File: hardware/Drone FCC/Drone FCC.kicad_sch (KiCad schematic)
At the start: 4 parts

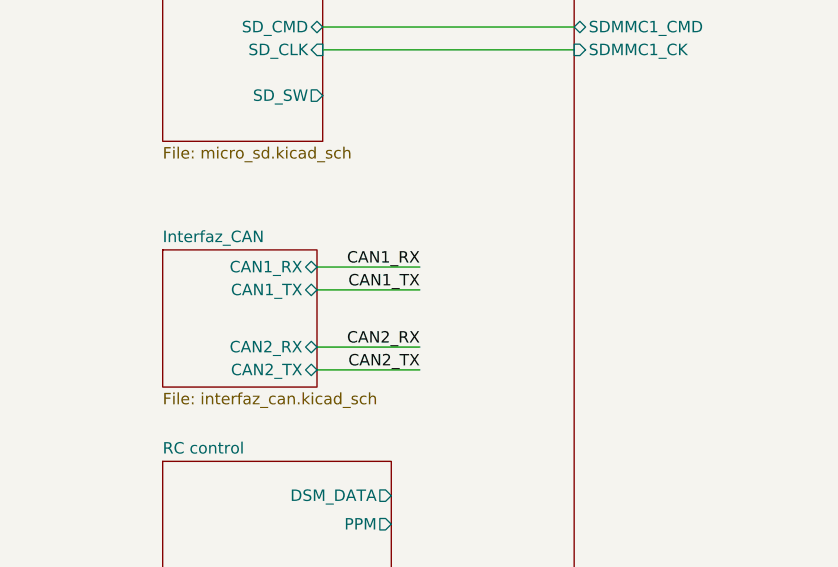
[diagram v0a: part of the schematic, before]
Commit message: add CAN schematic
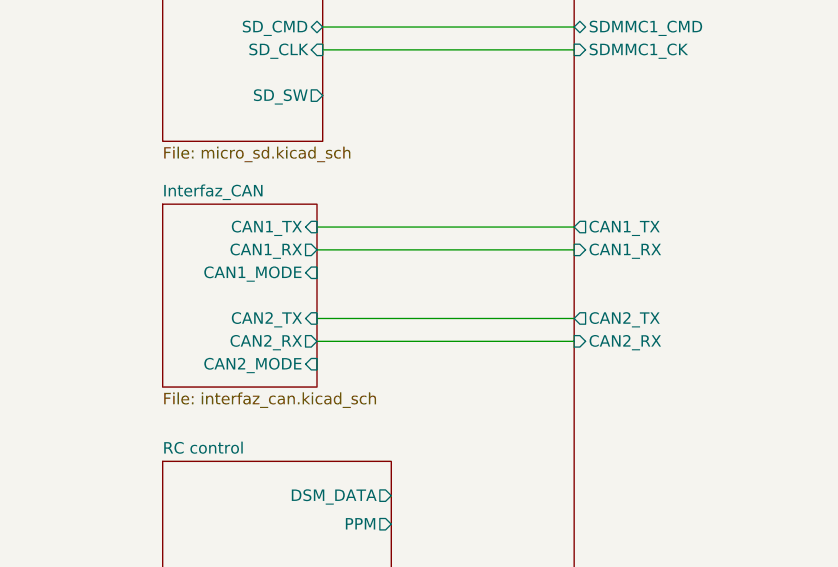
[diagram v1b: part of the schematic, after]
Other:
- sheet Interfaz_CAN ports: added CAN1_MODE, CAN2_MODE; removed none
- sheet MCU ports: added CAN1_RX, CAN1_TX, CAN2_RX, CAN2_TX; removed none

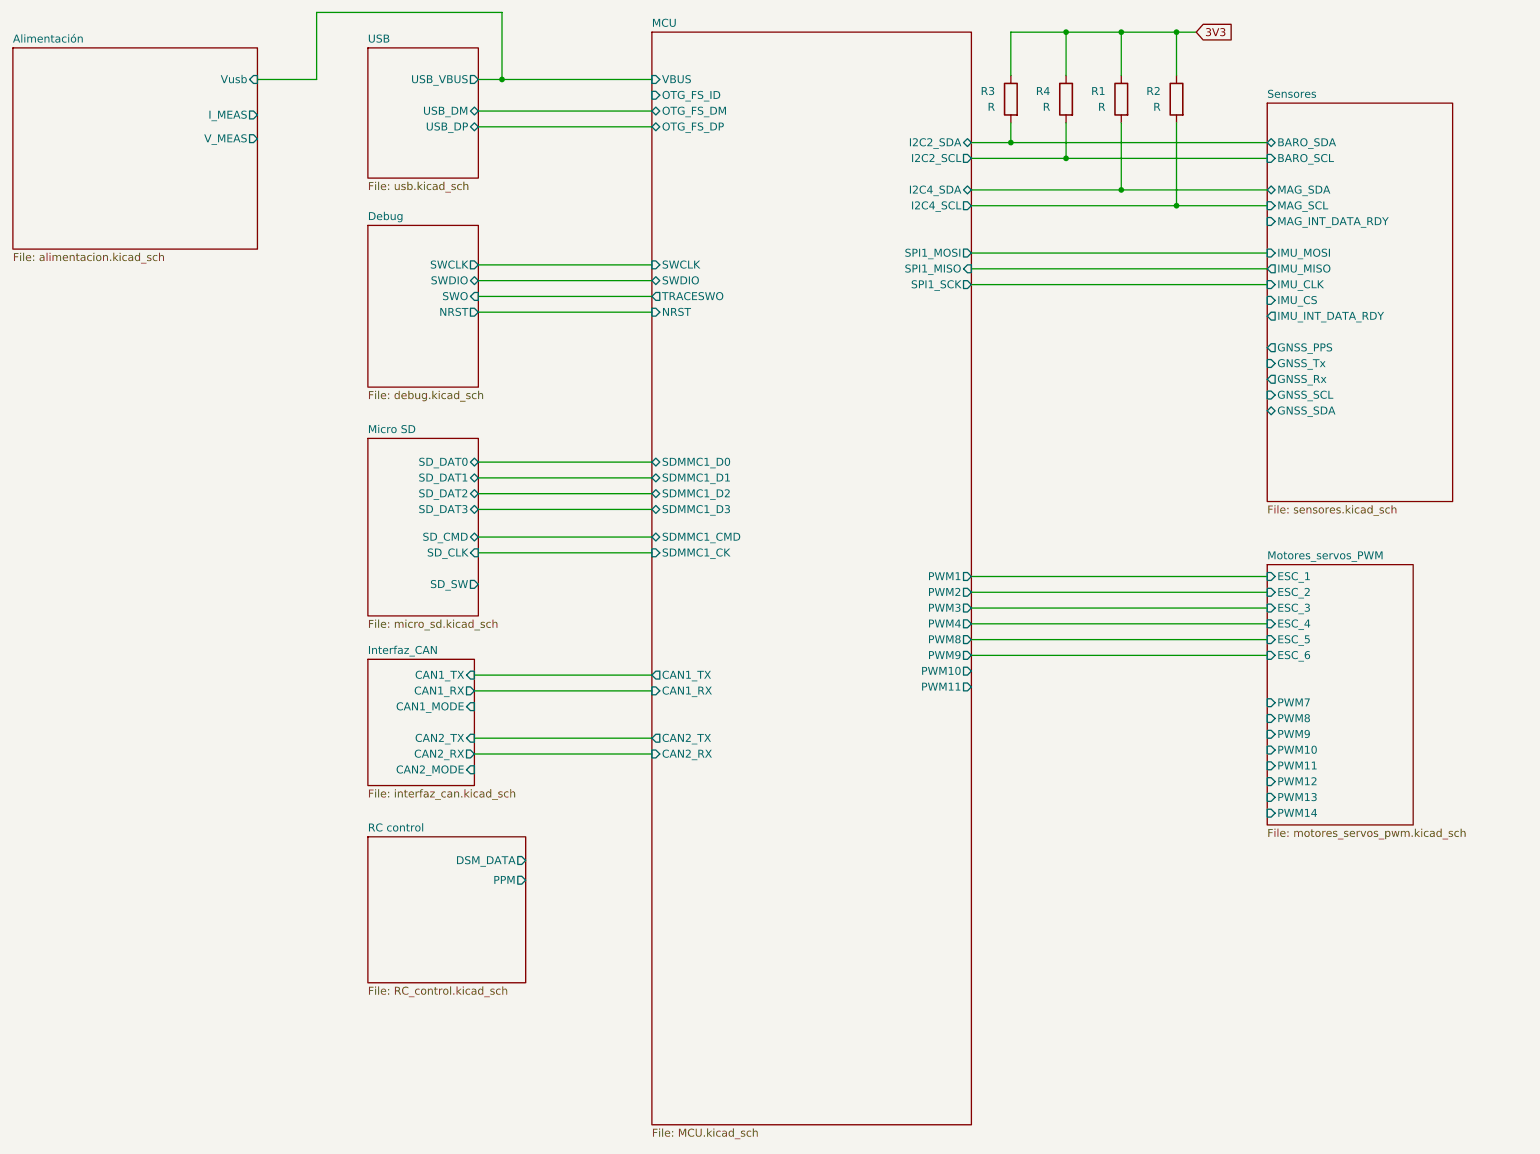
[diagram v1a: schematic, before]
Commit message: rearranged FCC schematic
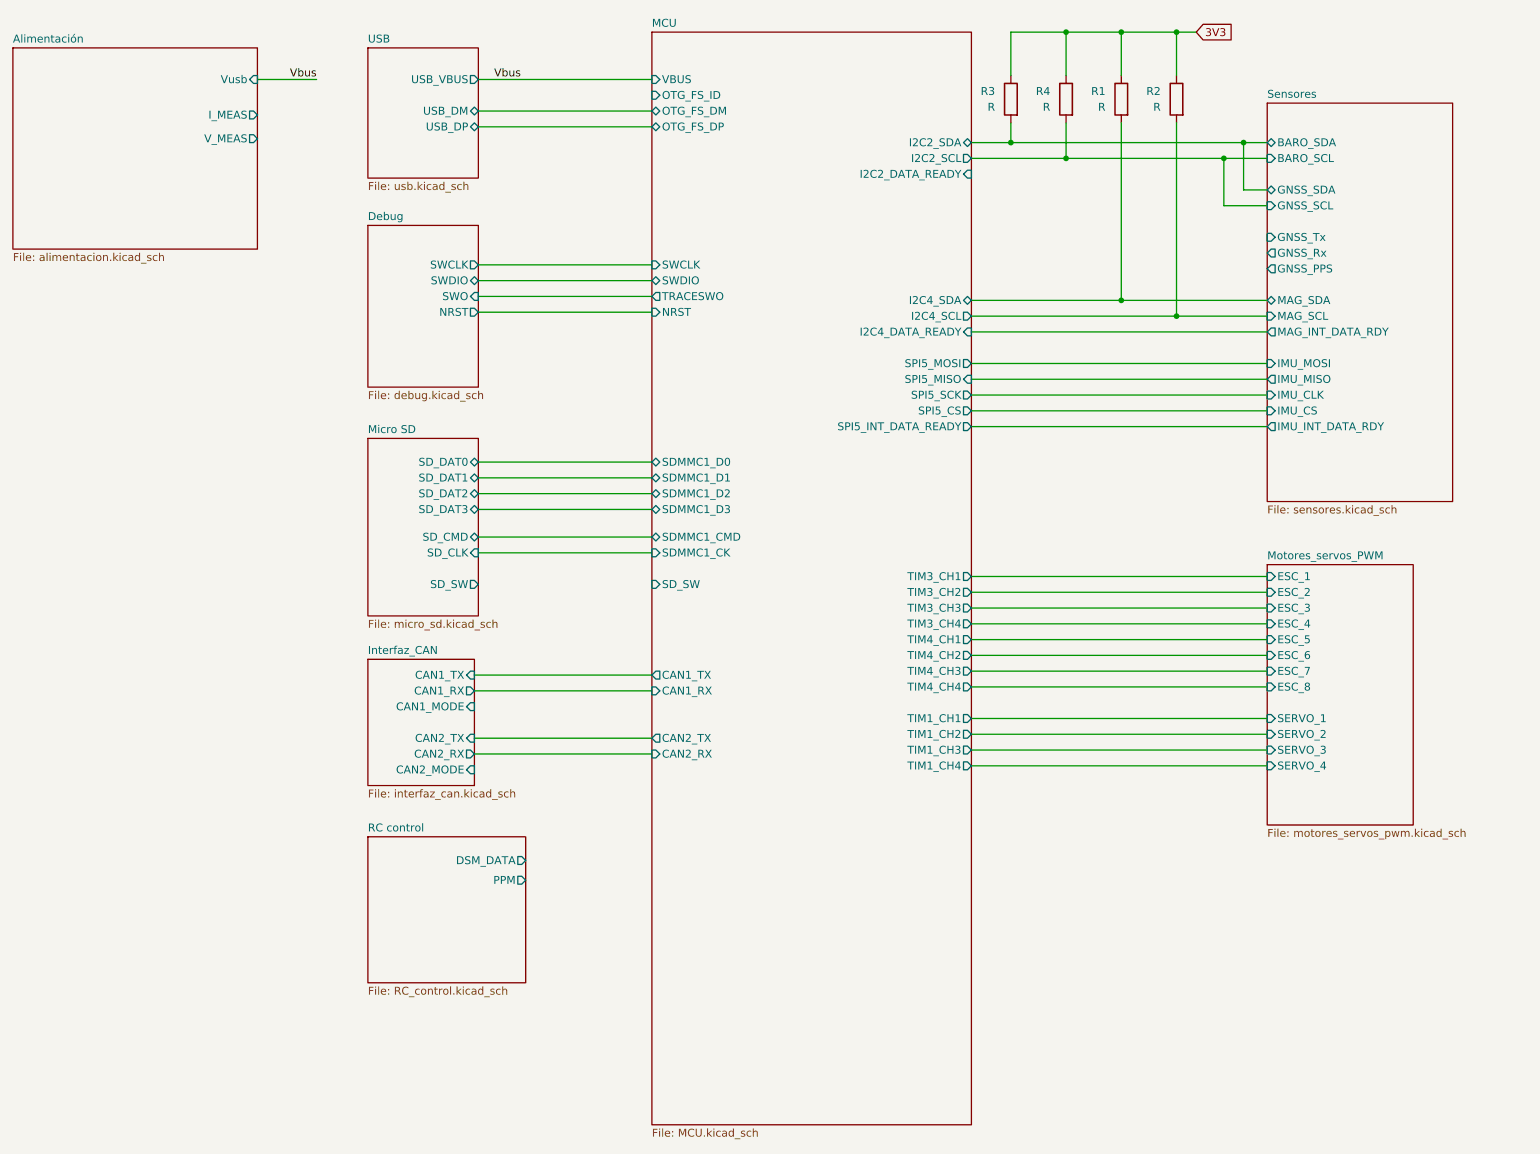
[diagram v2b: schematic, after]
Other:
- sheet MCU ports: added I2C2_DATA_READY, I2C4_DATA_READY, SD_SW, SPI5_CS, SPI5_INT_DATA_READY, SPI5_MISO, SPI5_MOSI, SPI5_SCK, TIM1_CH1, TIM1_CH2, TIM1_CH3, TIM1_CH4, TIM3_CH1, TIM3_CH2, TIM3_CH3, TIM3_CH4, TIM4_CH1, TIM4_CH2, TIM4_CH3, TIM4_CH4; removed PWM1, PWM10, PWM11, PWM2, PWM3, PWM4, PWM8, PWM9, SPI1_MISO, SPI1_MOSI, SPI1_SCK
- sheet Motores_servos_PWM ports: added ESC_7, ESC_8, SERVO_1, SERVO_2, SERVO_3, SERVO_4; removed PWM10, PWM11, PWM12, PWM13, PWM14, PWM7, PWM8, PWM9

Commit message: add external communication connectors
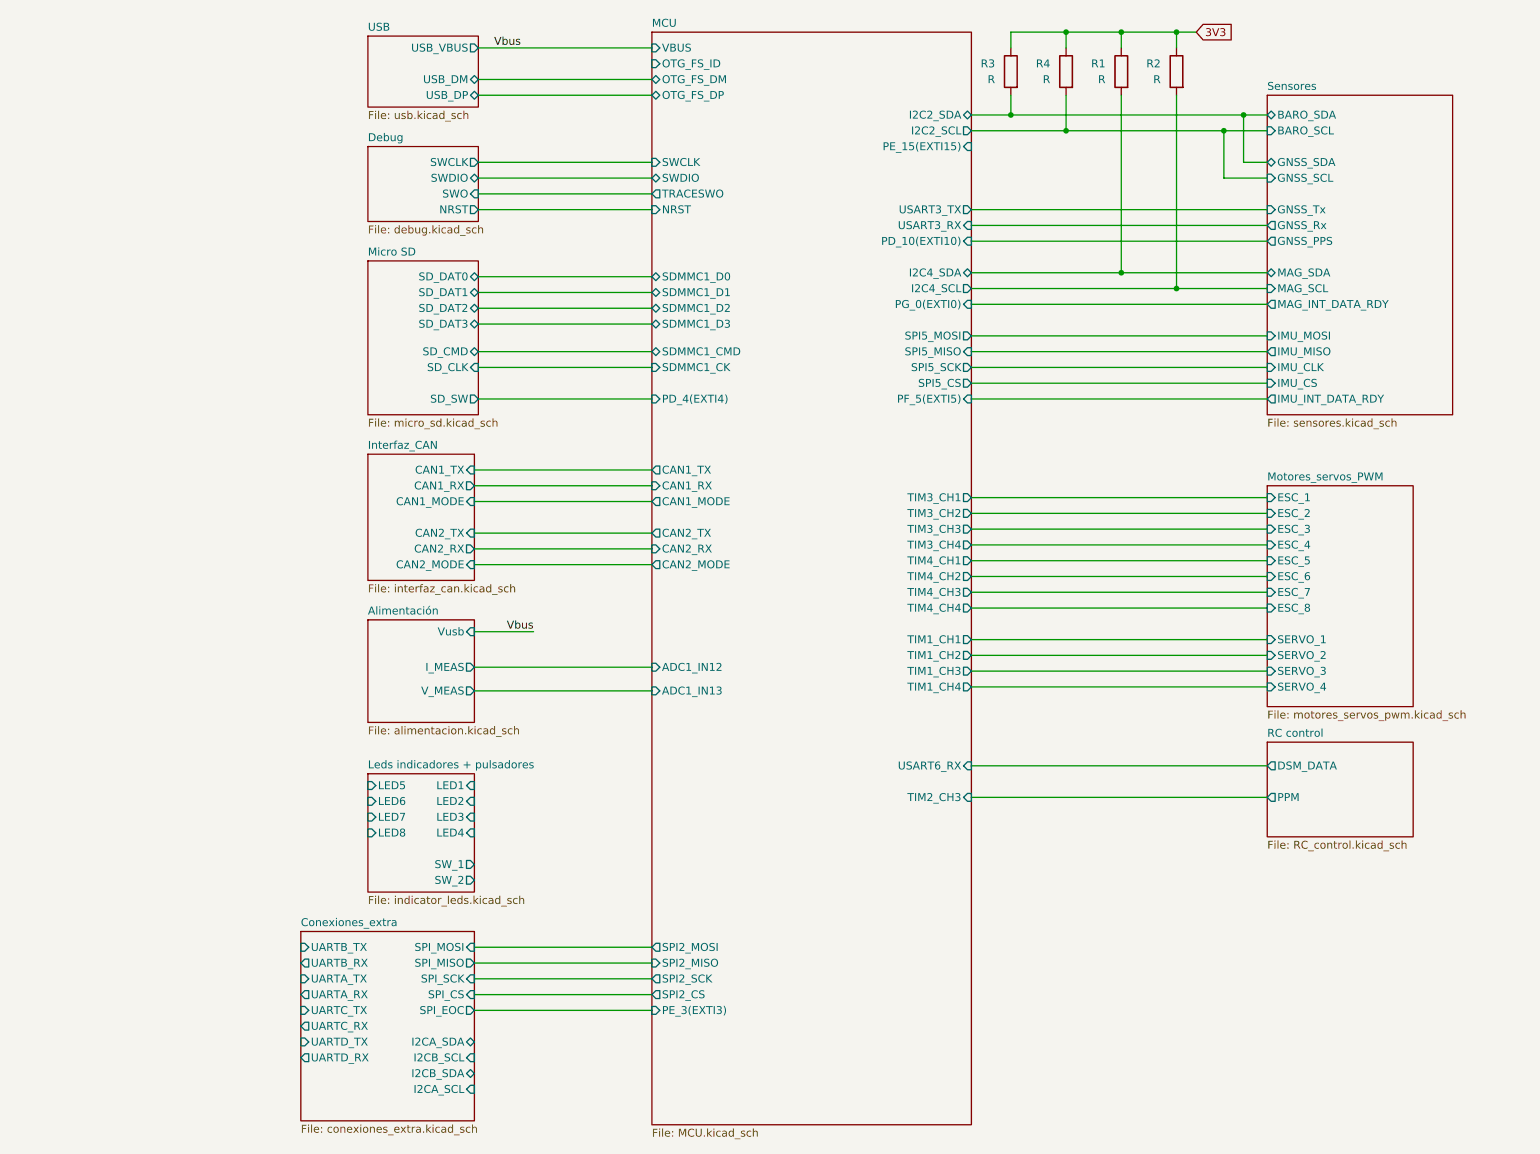
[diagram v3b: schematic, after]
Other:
- added sheet Conexiones_extra (conexiones_extra.kicad_sch)
- added sheet Leds indicadores + pulsadores (indicator_leds.kicad_sch)
- sheet MCU ports: added ADC1_IN12, ADC1_IN13, CAN1_MODE, CAN2_MODE, PD_10(EXTI10), PD_4(EXTI4), PE_15(EXTI15), PE_3(EXTI3), PF_5(EXTI5), PG_0(EXTI0), SPI2_CS, SPI2_MISO, SPI2_MOSI, SPI2_SCK, TIM2_CH3, USART3_RX, USART3_TX, USART6_RX; removed I2C2_DATA_READY, I2C4_DATA_READY, SD_SW, SPI5_INT_DATA_READY
- moved on the sheet: R1, R2, R3, R4

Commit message: re enumeration of components
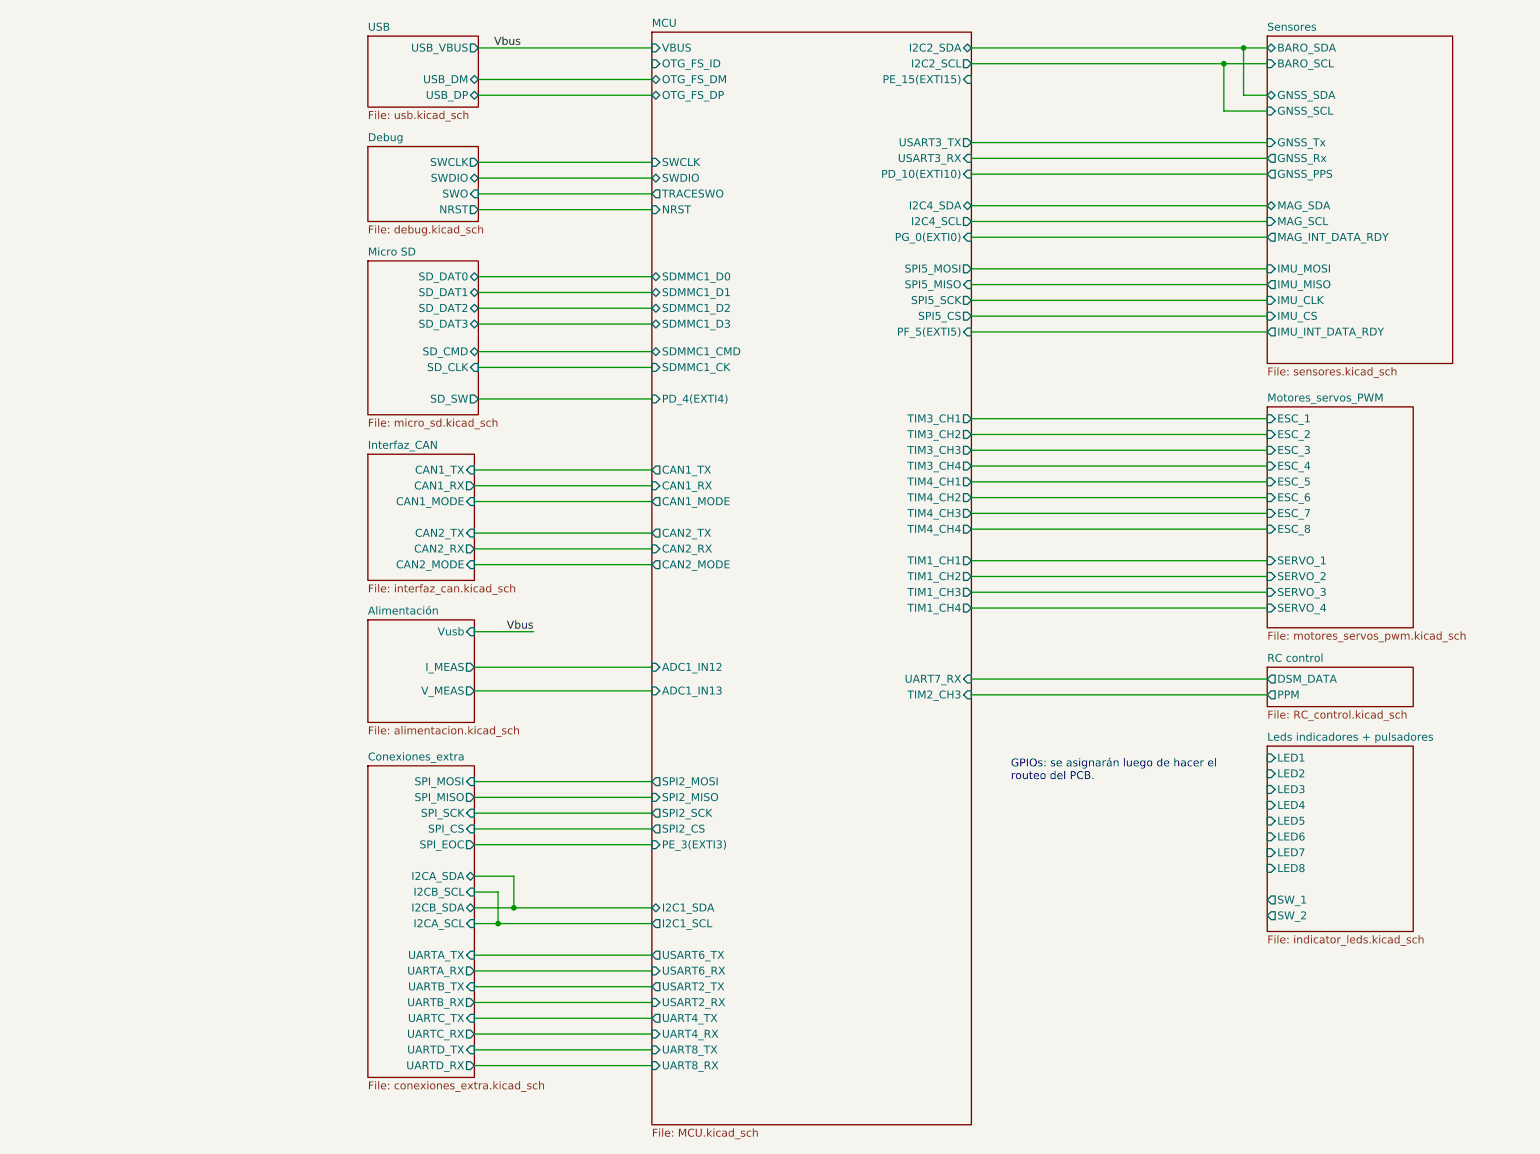
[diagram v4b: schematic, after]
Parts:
- removed R1, R2, R3, R4: R, symbol Device:R
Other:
- sheet MCU ports: added I2C1_SCL, I2C1_SDA, UART4_RX, UART4_TX, UART7_RX, UART8_RX, UART8_TX, USART2_RX, USART2_TX, USART6_TX; removed none
- note added: "GPIOs: se asignarán luego de hacer el routeo del PCB."

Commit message: start routing
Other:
- sheet MCU ports: added none; removed I2C1_SCL, I2C1_SDA

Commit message: continued preliminar routing
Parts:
- added C1, C2, C3, C4: 100nF, Capacitor_SMD:C_0603_1608Metric_Pad1.08x0.95mm_HandSolder, symbol Device:C_Small
- added H1, H2, H3, H4: MountingHole_Pad, MountingHole:MountingHole_3.2mm_M3_Pad_TopBottom, symbol Mechanical:MountingHole_Pad
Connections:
- new net: C2.1, H2.1
- new net: C1.1, H1.1
- new net: C4.1, H4.1
- new net: C3.1, H3.1
- new net GND: C1.2, C2.2, C3.2, C4.2
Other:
- sheet MCU ports: added TIM2_CH1, TIM2_CH2, TIM2_CH4; removed none

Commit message: continue routing
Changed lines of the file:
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@@
       (effects (font (size 1.27 1.27)) (justify right))
     )
-    (pin "TIM4_CH1" output (at 170.18 155.575 0)
+    (pin "TIM4_CH1" output (at 170.18 123.825 0)
       (effects (font (size 1.27 1.27)) (justify right))
     )
@@
       (effects (font (size 1.27 1.27)) (justify left))
     )
-    (pin "USART3_RX" input (at 170.18 47.625 0)
+    (pin "USART3_RX" input (at 170.18 121.285 0)
       (effects (font (size 1.27 1.27)) (justify right))
     )
-    (pin "USART3_TX" output (at 170.18 45.085 0)
+    (pin "USART3_TX" output (at 170.18 71.12 0)
       (effects (font (size 1.27 1.27)) (justify right))
     )
@@
       (effects (font (size 1.27 1.27)) (justify left))
     )
-    (pin "USART2_RX" input (at 118.745 173.355 180)
-      (effects (font (size 1.27 1.27)) (justify left))
+    (pin "USART2_RX" input (at 170.18 47.625 0)
+      (effects (font (size 1.27 1.27)) (justify right))
     )
-    (pin "USART2_TX" output (at 118.745 170.815 180)
-      (effects (font (size 1.27 1.27)) (justify left))
+    (pin "USART2_TX" output (at 170.18 45.085 0)
+      (effects (font (size 1.27 1.27)) (justify right))
     )
     (pin "UART4_RX" input (at 118.745 178.435 180)
@@
       (effects (font (size 1.27 1.27)) (justify left))
     )
-    (pin "UART7_RX" input (at 170.18 121.285 0)
+    (pin "UART7_RX" input (at 170.18 135.89 0)
       (effects (font (size 1.27 1.27)) (justify right))
     )

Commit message: routing: connected everything
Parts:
- removed C1, C2, C3, C4: 100nF, Capacitor_SMD:C_0603_1608Metric_Pad1.08x0.95mm_HandSolder, symbol Device:C_Small
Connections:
- net GND: now also H1.1, H2.1, H3.1, H4.1
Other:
- sheet Conexiones_extra ports: added none; removed UARTD_RX, UARTD_TX
- sheet MCU ports: added PG_2(EXTI2); removed PE_3(EXTI3), PG_0(EXTI0)
